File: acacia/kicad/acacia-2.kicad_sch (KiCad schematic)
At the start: 127 parts, among them J1 USB4500-03-0-A, SW1 A, SW10 C, SW11 R, SW12 F, SW13 V, SW14 T, SW15 G, SW16 Back, SW17 Gui, SW18 Ctl, SW19 Alt, SW2 Z, SW20 Sft, SW21 Fwd, SW22 AltGr, SW23 L2, SW24 L1, SW25 Ctl, SW26 U, SW27 J, SW28 M, SW29 N, SW3 Tab, SW30 Enter, SW31 I, SW32 K, SW33 Comm, SW34 O, SW35 L, SW36 Dot, SW38 P, SW39 Semi, SW4 B, SW40 Slsh, SW41 H, SW42 Y, SW43 QMK, SW48 Q, SW49 RESET, SW5 W, SW6 S, SW7 X, SW8 E, SW9 D, U1 USBLC6-2SC6, U2 ATmega32U2-A, Y1 16MHz

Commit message: wip
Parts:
- removed C7: 22p, Capacitor_SMD:C_0805_2012Metric_Pad1.18x1.45mm_HandSolder, symbol Device:C
- removed D20, D25, D30, D41: D, Diode_SMD:D_0805_2012Metric_Pad1.15x1.40mm_HandSolder, symbol Device:D
- removed SW20: Sft, mech-kbd:MX-Hotswap-1U, symbol Switch:SW_Push_45deg
- removed SW25: Ctl, mech-kbd:MX-Hotswap-1U, symbol Switch:SW_Push_45deg
- removed SW29: N, mech-kbd:MX-Hotswap-1U, symbol Switch:SW_Push_45deg
- removed SW30: Enter, mech-kbd:MX-Hotswap-1U, symbol Switch:SW_Push_45deg
- removed SW43: QMK, Button_Switch_SMD:SW_SPST_EVQQ2, symbol Switch:SW_Push
- removed TP5: C2, TestPoint:TestPoint_Pad_1.0x1.0mm, symbol Connector:TestPoint
- removed TP6: C4, TestPoint:TestPoint_Pad_1.0x1.0mm, symbol Connector:TestPoint
- removed TP7: C5, TestPoint:TestPoint_Pad_1.0x1.0mm, symbol Connector:TestPoint
- removed U2: ATmega32U2-A, Package_QFP:TQFP-32_7x7mm_P0.8mm, symbol MCU_Microchip_ATmega:ATmega32U2-A
- added C10: 4µ7, Capacitor_SMD:CP_Elec_8x6.9, symbol Device:C_Polarized
- added C7: 47µ, Capacitor_SMD:CP_Elec_8x6.9, symbol Device:C_Polarized
- added C9: 100n, Capacitor_SMD:C_0805_2012Metric_Pad1.18x1.45mm_HandSolder, symbol Device:C
- added FB3, FB4: 120@100M, Inductor_SMD:L_0805_2012Metric_Pad1.15x1.40mm_HandSolder, symbol Device:FerriteBead_Small
- added J2: 5V/0V, Connector_JST:JST_EH_B2B-EH-A_1x02_P2.50mm_Vertical, symbol Connector_Generic:Conn_01x02
- added U2: NCP1117, Package_TO_SOT_SMD:TO-252-2, symbol Regulator_Linear:NCP1117-3.3_TO252
- added U3: ATmega32U4-A, Package_QFP:TQFP-44_10x10mm_P0.8mm, symbol MCU_Microchip_ATmega:ATmega32U4-A
- SW12: value F -> T
- SW14: value T -> L1
- SW15: value G -> Prv
- SW16: value Back -> G
- SW17: value Gui -> B
- SW18: value Ctl -> Sft
- SW19: value Alt -> L2
- SW21: value Fwd -> H
- SW22: value AltGr -> K
- SW23: value L2 -> Spc
- SW24: value L1 -> Esc
- SW27: value J -> N
- SW32: value K -> E
- SW33: value Comm -> Com
- SW39: value Semi -> Y
- SW4: value B -> Nxt
- SW40: value Slsh -> J
- SW41: value H -> Del
- SW42: value Y -> Ent
- SW8: value E -> F
- TP1: value GND -> GNDD
- TP3: value D0 -> 5V; footprint TestPoint:TestPoint_Pad_1.0x1.0mm -> TestPoint:TestPoint_Pad_1.5x1.5mm
- TP4: value D1 -> 3V3; footprint TestPoint:TestPoint_Pad_1.0x1.0mm -> TestPoint:TestPoint_Pad_1.5x1.5mm
- Y1: value 16MHz -> 8MHz
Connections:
- net R4 is gone; now on net R3: D15.1 (K), D4.1 (K)
- net +5V: now also FB2.2, C9.1, U2.3 (VI), U3.2 (UVCC), U3.7 (VBUS); no longer C8.1, F1.2, R4.1
- net C0: now also U3.25 (PD4); no longer SW4.2
- net C1: now also U3.21 (PD3)
- net C2: now also SW15.2, U3.20 (PD2)
- net C3: now also U3.32 (PC7); no longer SW15.2
- net C4: now also U3.31 (PC6)
- net C5: now also U3.39 (PF4)
- net C6: now also U3.26 (PD6)
- net C7: now also SW4.2, U3.27 (PD7)
- net C8: now also U3.40 (PF1)
- net C9: now also U3.41 (PF0)
- net DDDD+: now also U3.4 (D+)
- net DDDD-: now also U3.3 (D-)
- net GND: now also C2.1, FB1.2, R1.1; no longer C1.1, C3.2, C4.2, C5.2, C6.2, C8.2, FB1.1, R6.2, SW49.2, TP1.1
- net R0: now also U3.22 (PD5)
- net R1: now also U3.38 (PF5)
- net R2: now also U3.37 (PF6)
- net R3: now also U3.36 (PF7)
- net VBUS: now also F1.1; no longer FB2.1
- net at C3.1, Y1.1: now also U3.17 (XTAL1)
- net at R6.1: now also U3.33 (~{HWB}/PE2)
- net at C4.1, Y1.2: now also U3.16 (XTAL2)
- net at C5.1: now also U3.6 (UCAP)
- net at TP3.1: now also C7.1, FB4.2
- net +3V3: now reaches TP4.1
- net +3V3: now also C8.1, R4.1, C10.1, U2.2 (VO), U3.14 (VCC), U3.24 (AVCC), U3.34 (VCC), U3.44 (AVCC)
- net at R4.2, R5.1: now also SW49.1
- net ~{RESET}: no longer names the net of R5.2
- net ~{RESET}: now also U3.13 (~{RESET}); no longer SW49.1
- new net: FB3.2, J2.1 (Pin_1)
- new net: FB4.1, J2.2 (Pin_2)
- new net: C1.2, F1.2, FB2.1
- new net GNDD: C1.1, C10.2, C3.2, C4.2, C5.2, C6.2, C7.2, C8.2, C9.2, FB1.1, FB3.1, R6.2, SW49.2, TP1.1, U2.1 (GND), U3.15 (GND), U3.23 (GND), U3.35 (GND), U3.43 (GND), U3.5 (UGND)
- new net MISO: U3.11 (PB3)
- new net MOSI: U3.10 (PB2)
- new net SCK: U3.9 (PB1)
- new net SCL: U3.18 (PD0)
- new net SDA: U3.19 (PD1)
- no-connect marks 2 -> 3
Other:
- note added: "Dropout 1V2"
- moved on the sheet: C1, C2, C3, C4, C5, C6, C8, D15, F1, FB1, FB2, FL1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

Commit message: WIP: v2 board
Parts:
- removed C10: 4µ7, Capacitor_SMD:CP_Elec_8x6.9, symbol Device:C_Polarized
- removed C7: 47µ, Capacitor_SMD:CP_Elec_8x6.9, symbol Device:C_Polarized
- removed C9: 100n, Capacitor_SMD:C_0805_2012Metric_Pad1.18x1.45mm_HandSolder, symbol Device:C
- removed FB3, FB4: 120@100M, Inductor_SMD:L_0805_2012Metric_Pad1.15x1.40mm_HandSolder, symbol Device:FerriteBead_Small
- removed J2: 5V/0V, Connector_JST:JST_EH_B2B-EH-A_1x02_P2.50mm_Vertical, symbol Connector_Generic:Conn_01x02
- removed TP3: 5V, TestPoint:TestPoint_Pad_1.5x1.5mm, symbol Connector:TestPoint
- removed TP4: 3V3, TestPoint:TestPoint_Pad_1.5x1.5mm, symbol Connector:TestPoint
- removed U2: NCP1117, Package_TO_SOT_SMD:TO-252-2, symbol Regulator_Linear:NCP1117-3.3_TO252
- added C6: 1µ, Capacitor_SMD:C_0805_2012Metric_Pad1.18x1.45mm_HandSolder, symbol Device:C
- added D39, D40, D41, D42, D43: SK6805, LED_SMD:LED_SK6805_PLCC4_2.4x2.7mm_P1.3mm, symbol LED:SK6805
- added J1: Trackpad, Connector:FanPinHeader_1x04_P2.54mm_Vertical, symbol Connector:Conn_01x04_Socket
- SW32: renamed from SW3; footprint mech-kbd:MX-Hotswap-1U -> mech-kbd:MX-Hotswap-1.5U
- SW33: renamed from SW15; footprint mech-kbd:MX-Hotswap-1U -> mech-kbd:MX-Hotswap-1.5U
- SW35: renamed from SW19; footprint mech-kbd:MX-Hotswap-1.25U -> mech-kbd:MX-Hotswap-1.5U
- SW36: renamed from SW24; footprint mech-kbd:MX-Hotswap-1.25U -> mech-kbd:MX-Hotswap-1.5U
- SW38: renamed from SW4; footprint mech-kbd:MX-Hotswap-1U -> mech-kbd:MX-Hotswap-1.5U
- SW39: renamed from SW42; footprint mech-kbd:MX-Hotswap-1U -> mech-kbd:MX-Hotswap-1.5U
- Y1: value 8MHz -> 16MHz
- renumbered C6 to C1, C8 to C2, C1 to C7, C2 to C8, D48 to D1, D37 to D10, D1 to D11, D6 to D12, D9 to D13, D12 to D14, D17 to D15, D22 to D16, D27 to D17, D32 to D18, D35 to D19, D5 to D2, D38 to D20, D2 to D21, D7 to D22, D10 to D23, D13 to D24, D18 to D25, D23 to D26, D28 to D27, D33 to D28, D36 to D29, D8 to D3, D39 to D30, D3 to D31, D15 to D32, D14 to D33, D19 to D34, D24 to D35, D29 to D36, D4 to D37, D40 to D38, D11 to D4, D16 to D5, D21 to D6, D26 to D7, D31 to D8, D34 to D9, FB2 to FB1, FB1 to FB2, H5 to H3, H8 to H4, H3 to H5, H9 to H7, H4 to H8, H7 to H9, J1 to J2, R4 to R1, R5 to R2, R6 to R3, R7 to R4, R8 to R5, R2 to R6, R3 to R7, R1 to R8, SW48 to SW1, SW38 to SW10, SW1 to SW11, SW6 to SW12, SW9 to SW13, SW12 to SW14, SW17 to SW15, SW22 to SW16, SW27 to SW17, SW32 to SW18, SW35 to SW19, SW5 to SW2, SW39 to SW20, SW49 to SW21, SW2 to SW22, SW7 to SW23, SW10 to SW24, SW13 to SW25, SW18 to SW26, SW23 to SW27, SW33 to SW29, SW8 to SW3, SW36 to SW30, SW40 to SW31, SW14 to SW34, SW41 to SW37, SW11 to SW4, SW16 to SW5, SW21 to SW6, SW26 to SW7, SW31 to SW8, SW34 to SW9, TP2 to TP1, TP1 to TP2, U3 to U1, U1 to U2
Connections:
- net +3V3 is gone; now on net +5V: C2.1, R1.1, U1.14 (VCC), U1.24 (AVCC), U1.34 (VCC), U1.44 (AVCC)
- net +5V: now also C6.1, D39.4 (VDD), D40.4 (VDD), D41.4 (VDD), D42.4 (VDD), D43.4 (VDD), J1.1 (Pin_1)
- net GNDD: now also C6.2, D39.2 (VSS), D40.2 (VSS), D41.2 (VSS), D42.2 (VSS), D43.2 (VSS), J1.4 (Pin_4)
- net SCL: now also J1.2 (Pin_2)
- net SDA: now also J1.3 (Pin_3)
- net RGB: now reaches U1.8 (PB0)
- net RGB: now also D39.3 (DIN)
- net MISO: no longer names the net of U1.11 (PB3)
- net MOSI: no longer names the net of U1.10 (PB2)
- net SCK: no longer names the net of U1.9 (PB1)
- new net: D40.1 (DOUT), D41.3 (DIN)
- new net: D39.1 (DOUT), D40.3 (DIN)
- new net: D41.1 (DOUT), D42.3 (DIN)
- new net: D42.1 (DOUT), D43.3 (DIN)
- no-connect marks 3 -> 4
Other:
- note removed: "Dropout 1V2"
- moved on the sheet: C1, C2, C3, C4, C5, C7, C8, D1, D10, D11, D12, D13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

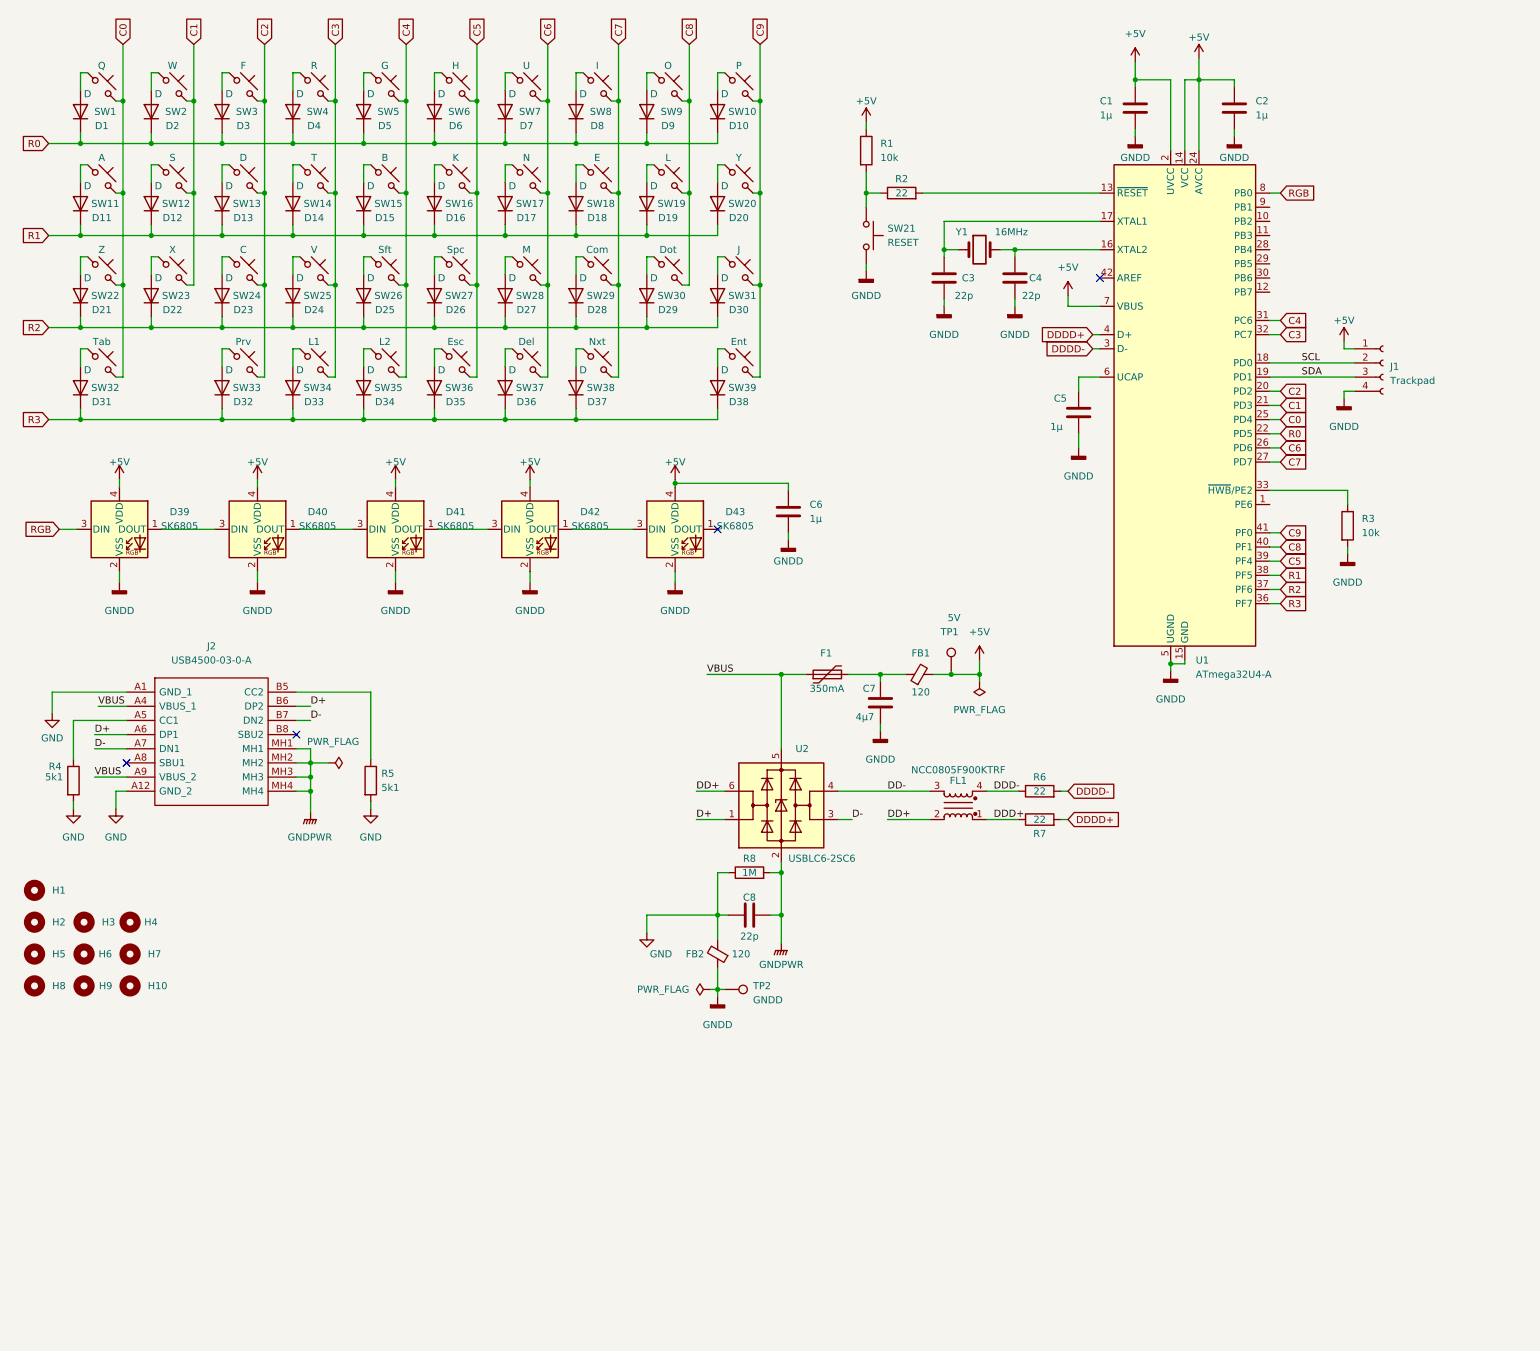
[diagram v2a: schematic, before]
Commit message: New USB connector
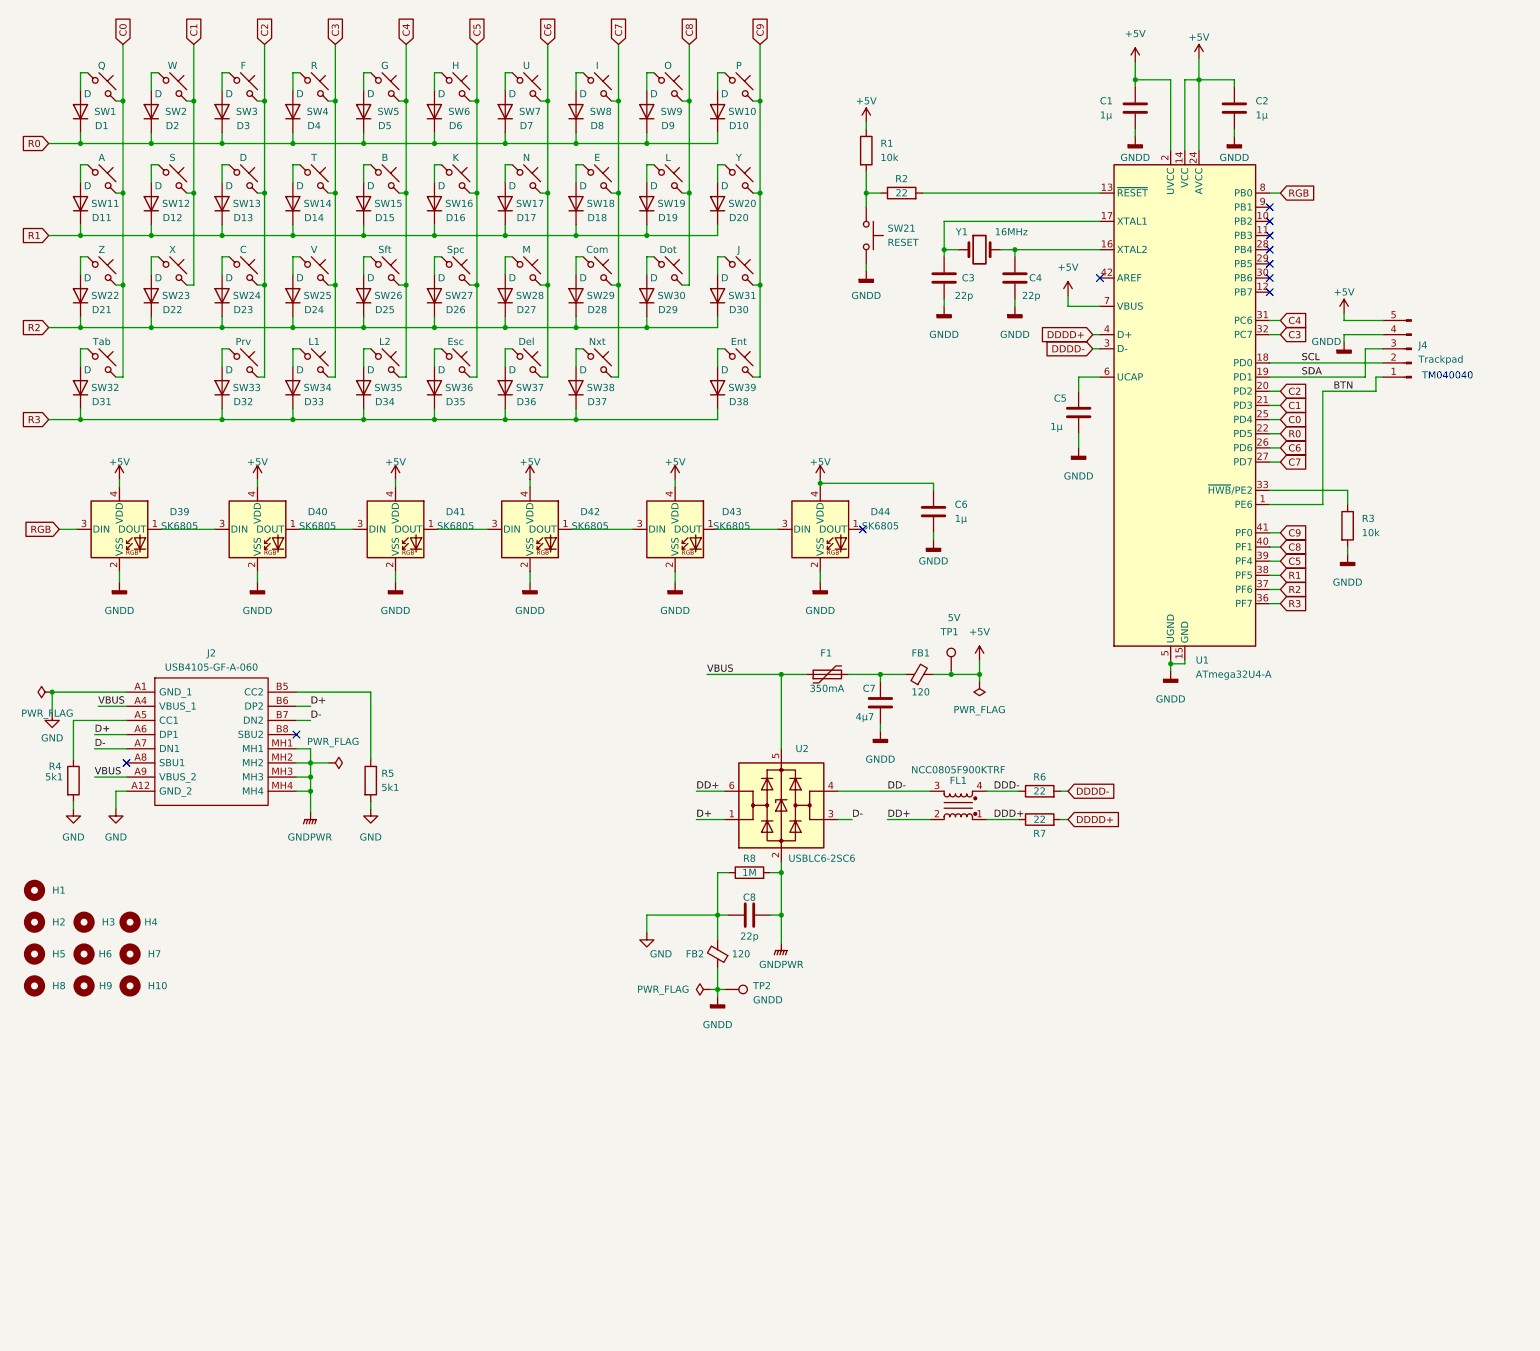
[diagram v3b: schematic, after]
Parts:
- removed J1: Trackpad, Connector:FanPinHeader_1x04_P2.54mm_Vertical, symbol Connector:Conn_01x04_Socket
- added D43: SK6805, LED_SMD:LED_SK6805_PLCC4_2.4x2.7mm_P1.3mm, symbol LED:SK6805
- added J4: Trackpad, symbol Connector:Conn_01x05_Pin
- J2: value USB4500-03-0-A -> USB4105-GF-A-060; footprint mech-kbd:USB4500030A -> mech-kbd:GCT_USB4105-GF-A
- renumbered D43 to D44
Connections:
- net +5V: now also D43.4 (VDD), J4.5 (Pin_5)
- net GNDD: now also D43.2 (VSS), J4.4 (Pin_4)
- net SCL: now also J4.2 (Pin_2)
- net SDA: now also J4.3 (Pin_3)
- net BTN: now reaches U1.1 (PE6)
- net BTN: now also J4.1 (Pin_1)
- net at D44.3 (DIN): now also D43.1 (DOUT); no longer D42.1 (DOUT)
- new net: D42.1 (DOUT), D43.3 (DIN)
- no-connect marks 4 -> 11
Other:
- note added: "TM040040"
- moved on the sheet: C6, D44

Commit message: qwerty layout
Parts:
- removed J4: Trackpad, symbol Connector:Conn_01x05_Pin
- added J1: TM040040, symbol Connector:Conn_01x12_Socket
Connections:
- net +5V: now also J1.1 (Pin_1)
- net BTN: now also J1.5 (Pin_5)
- net GNDD: now also J1.2 (Pin_2)
- net SCL: now also J1.4 (Pin_4)
- net SDA: now also J1.3 (Pin_3)
- no-connect marks 11 -> 16
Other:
- note removed: "TM040040"
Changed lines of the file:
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@@
   (junction (at 148.59 63.5) (diameter 0) (color 0 0 0 0)
   )
+  (no_connect (at 260.35 95.25))
   (no_connect (at 240.03 64.77))
+  (no_connect (at 260.35 87.63))
   (no_connect (at 34.925 149.225))
   (no_connect (at 209.55 62.23))
@@
   (no_connect (at 240.03 57.15))
   (no_connect (at 65.405 144.145))
+  (no_connect (at 260.35 97.79))
   (no_connect (at 167.005 107.315))
+  (no_connect (at 260.35 92.71))
   (no_connect (at 240.03 59.69))
+  (no_connect (at 260.35 90.17))
   (no_connect (at 240.03 62.23))
   (no_connect (at 240.03 49.53))
@@
     (stroke (width 0) (type default))
   )
-  (text "TM040040" (at 267.335 80.645 0)
-    (effects (font (size 1.27 1.27)) (justify left bottom))
-  )
   (label "DD+" (at 137.16 154.305 0) (fields_autoplaced)
     (effects (font (size 1.27 1.27)) (justify left bottom))
@@
     )
   )
-  (symbol (lib_id "Connector:Conn_01x05_Pin") (at 265.43 74.93 180) (unit 1)
-    (in_bom yes) (on_board yes) (dnp no) (fields_autoplaced)
-    (property "Reference" "J4" (at 266.7 74.295 0)
-      (effects (font (size 1.27 1.27)) (justify right))
-    )
-    (property "Value" "Trackpad" (at 266.7 76.835 0)
-      (effects (font (size 1.27 1.27)) (justify right))
-    )
-    (property "Footprint" "" (at 265.43 74.93 0)
-      (effects (font (size 1.27 1.27)) hide)
-    )
-    (property "Datasheet" "~" (at 265.43 74.93 0)
-      (effects (font (size 1.27 1.27)) hide)
-    )
-    (pin "1")
-    (pin "2")
-    (pin "3")
-    (pin "4")
-    (pin "5")
-    (instances
-      (project "acacia-2"
-        (path "/c5eaf993-5ca3-41a9-9f58-50b86c0038a2"
-          (reference "J4") (unit 1)
-        )
-      )
-    )
-  )
   (symbol (lib_id "Switch:SW_Push_45deg") (at 43.18 44.45 0) (unit 1)
     (in_bom yes) (on_board yes) (dnp no)
@@
         )
       )
+    )
+  )
+  (symbol (lib_id "Connector:Conn_01x12_Socket") (at 265.43 82.55 0) (unit 1)
+    (in_bom yes) (on_board yes) (dnp no) (fields_autoplaced)
+    (property "Reference" "J1" (at 266.7 82.55 0)
+      (effects (font (size 1.27 1.27)) (justify left))
+    )
+    (property "Value" "TM040040" (at 266.7 85.09 0)
+      (effects (font (size 1.27 1.27)) (justify left))
+    )
+    (property "Footprint" "" (at 265.43 82.55 0)
+      (effects (font (size 1.27 1.27)) hide)
+    )
+    (property "Datasheet" "~" (at 265.43 82.55 0)
+      (effects (font (size 1.27 1.27)) hide)
+    )
+    (pin "1")
+    (pin "10")
+    (pin "11")
+    (pin "12")
+    (pin "2")
+    (pin "3")
+    (pin "4")
+    (pin "5")
+    (pin "6")
+    (pin "7")
+    (pin "8")
+    (pin "9")
+    (instances
+      (project "acacia-2"
+        (path "/c5eaf993-5ca3-41a9-9f58-50b86c0038a2"
+          (reference "J1") (unit 1)
+        )
+      )

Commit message: Symbols
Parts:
- added J3: GroveMiniTrack, symbol Connector:Conn_01x04_Socket
- added R10, R9: 22, symbol Device:R
- SW14: value T -> F
- SW15: value B -> G
- SW16: value K -> H
- SW17: value N -> J
- SW18: value E -> K
- SW20: value Y -> B
- SW28: value M -> N
- SW29: value Com -> M
- SW3: value F -> E
- SW30: value Dot -> Com
- SW31: value J -> Dot
- SW35: value L2 -> AGr
- SW5: value G -> T
- SW6: value H -> Y
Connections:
- net +5V: now also J3.2 (Pin_2)
- net GNDD: now also J3.1 (Pin_1)
- net SCL: now also J3.3 (Pin_3), J3.4 (Pin_4), R10.2; no longer U1.18 (PD0)
- net SDA: now also R9.2; no longer U1.19 (PD1)
- new net: R10.1, U1.18 (PD0)
- new net: R9.1, U1.19 (PD1)
- no-connect marks 16 -> 18
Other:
- moved on the sheet: J1

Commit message: WIP
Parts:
- F1: footprint Resistor_SMD:R_1210_3225Metric_Pad1.30x2.65mm_HandSolder -> Resistor_SMD:R_1206_3216Metric_Pad1.30x1.75mm_HandSolder
- J1: renamed from J3; footprint (none) -> Connector_JST:JST_XA_B04B-XASK-1-A_1x04_P2.50mm_Vertical
- J2: renamed from J1; footprint (none) -> Connector_FFC-FPC:Hirose_FH12-12S-0.5SH_1x12-1MP_P0.50mm_Horizontal
- R3: renamed from R10; footprint (none) -> Resistor_SMD:R_0805_2012Metric_Pad1.20x1.40mm_HandSolder
- R4: renamed from R9; footprint (none) -> Resistor_SMD:R_0805_2012Metric_Pad1.20x1.40mm_HandSolder
- TP1, TP2: footprint TestPoint:TestPoint_Pad_1.0x1.0mm -> TestPoint:TestPoint_Pad_D1.5mm
- renumbered J2 to J3, R8 to R10, R3 to R5, R4 to R6, R5 to R7, R6 to R8, R7 to R9
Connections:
- net +5V: now also J2.12 (Pin_12); no longer J2.1 (Pin_1)
- net BTN: now also J2.8 (Pin_8); no longer J2.5 (Pin_5)
- net D+: now also U2.3 (I/O2); no longer U2.1 (I/O1)
- net D-: now also U2.1 (I/O1); no longer U2.3 (I/O2)
- net DD+: now also FL1.3, U2.4 (I/O2); no longer FL1.2, U2.6 (I/O1)
- net DD-: now also FL1.2, U2.6 (I/O1); no longer FL1.3, U2.4 (I/O2)
- net DDD+: now also FL1.4, R8.1; no longer FL1.1, R9.1
- net DDD-: now also FL1.1, R9.1; no longer FL1.4, R8.1
- net DDDD+: now also R8.2; no longer R9.2
- net DDDD-: now also R9.2; no longer R8.2
- net GNDD: now also J2.11 (Pin_11); no longer J2.2 (Pin_2)
- net GNDPWR: now also J3.S1 (MH1), J3.S2 (MH2), J3.S3 (MH3), J3.S4 (MH4); no longer J3.MH1, J3.MH2, J3.MH3, J3.MH4
- net SCL: now also J2.9 (Pin_9); no longer J2.4 (Pin_4)
- net SDA: now also J2.10 (Pin_10); no longer J2.3 (Pin_3)
